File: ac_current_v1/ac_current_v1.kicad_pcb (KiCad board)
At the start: 2 copper layers, 107.7 x 89.4 mm, 35 parts, among them J1 ICSP, J2 UART, J3 AC1_IN, J4 AC1_OUT, J5 AC2_IN, J6 AC2_OUT, J7 GMS1012, J8 AC_SLCT_2, J9 AC_SLCT_1, U1 NRF24L01_Breakout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

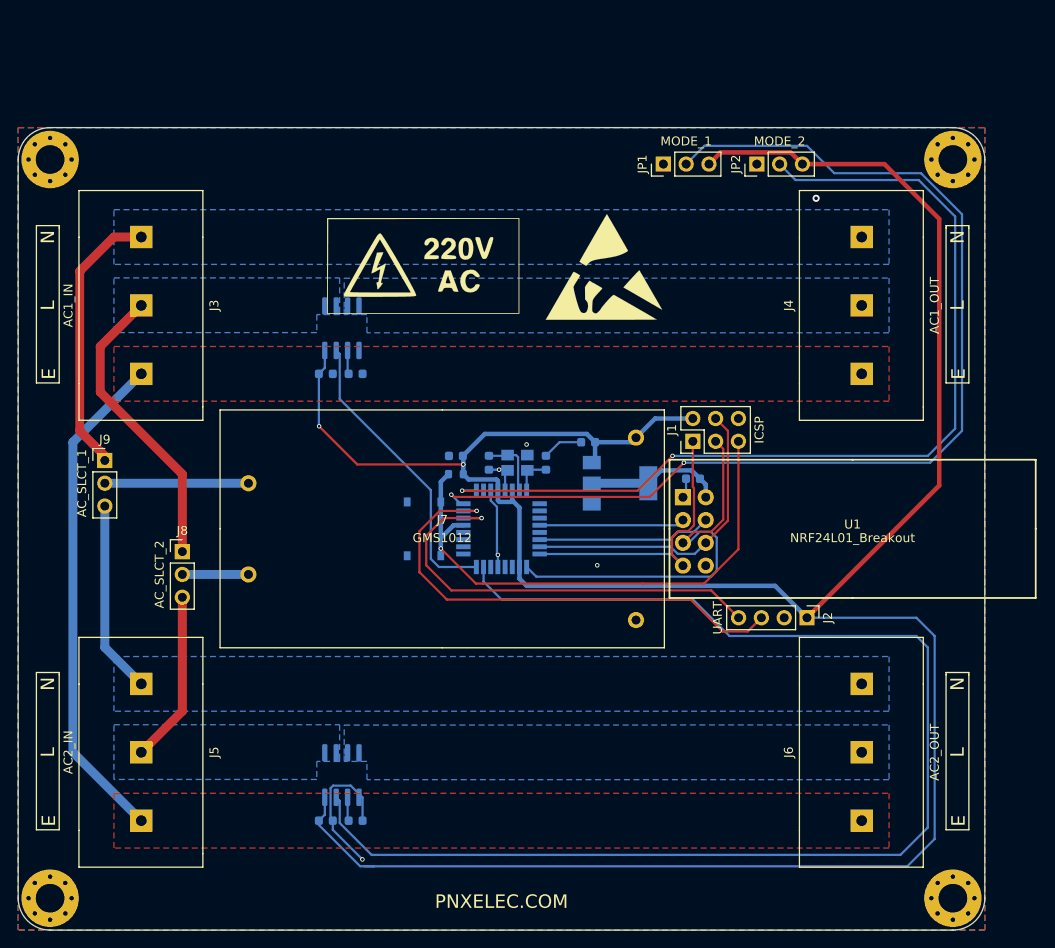
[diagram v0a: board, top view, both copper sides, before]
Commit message: PCB Update(Added Sensor)
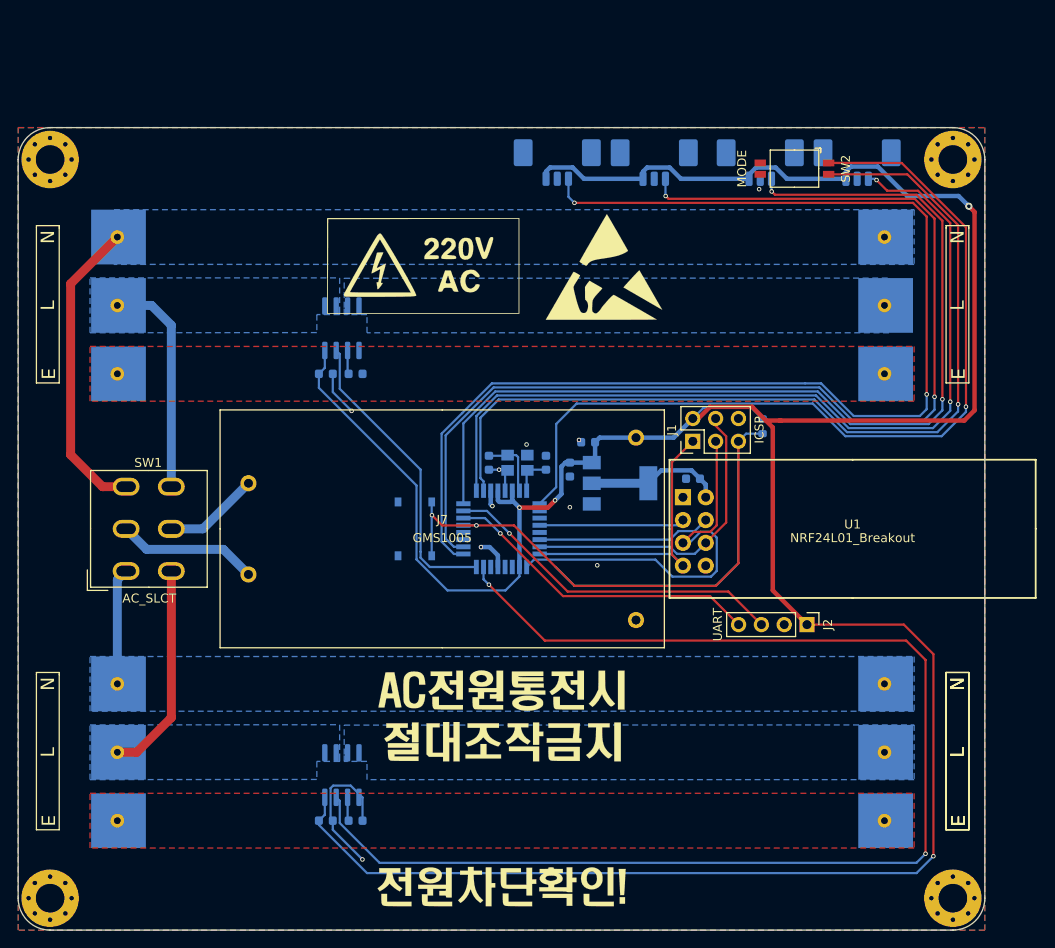
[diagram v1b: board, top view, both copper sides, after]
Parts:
- removed J8: AC_SLCT_2, Connector_PinHeader_2.54mm:PinHeader_1x03_P2.54mm_Vertical
- removed J9: AC_SLCT_1, Connector_PinHeader_2.54mm:PinHeader_1x03_P2.54mm_Vertical
- removed JP1: MODE_1, Connector_PinHeader_2.54mm:PinHeader_1x03_P2.54mm_Vertical
- removed JP2: MODE_2, Connector_PinHeader_2.54mm:PinHeader_1x03_P2.54mm_Vertical
- added G***: LOGO, KIcad:caution2, F.Cu at (150.2, 140.1)
- added G***: LOGO, KIcad:caution, F.Cu at (150.2, 121.0)
- added J10: Flow_1, Connector_Molex:Molex_PicoBlade_53261-0371_1x03-1MP_P1.25mm_Horizontal, B.Cu at (189.9, 58.8)
- added J11: Flow_2, Connector_Molex:Molex_PicoBlade_53261-0371_1x03-1MP_P1.25mm_Horizontal, B.Cu at (179.1, 58.8)
- added J12: NC_Liquid_1, Connector_Molex:Molex_PicoBlade_53261-0371_1x03-1MP_P1.25mm_Horizontal, B.Cu at (167.3, 58.8)
- added J13: NC_Liquid_2, Connector_Molex:Molex_PicoBlade_53261-0371_1x03-1MP_P1.25mm_Horizontal, B.Cu at (156.5, 58.8)
- added SW1: AC_SLCT, KIcad:MTS-202, F.Cu at (111.0, 100.2)
- added SW2: MODE, KIcad:DSHP02TSGER, F.Cu at (182.9, 60.1)
- J3, J4, J5, J6: footprint KIcad:BR-762C_3 -> KIcad:SMD_762; moved to B.Cu
- J7: value GMS1012 -> GMS1005
- moved R1 34.6 mm to (179.3, 88.8), turned to 90 degrees
- moved C3 12.8 mm to (157.9, 93.6), turned to 90 degrees
- moved J4 5.20 mm to (193.0, 75.3)
- moved J6 5.20 mm to (193.0, 125.1)
- moved S1 1.02 mm to (140.6, 100.2)
- moved J2 0.76 mm to (184.3, 110.9)
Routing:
- net /A2: track 0.00 -> 137.5 mm, vias 0 -> 2
- net /A3: track 0.00 -> 126.7 mm, vias 0 -> 2
- net /D4: track 0.00 -> 102.3 mm, vias 0 -> 1
- net /D5: track 0.00 -> 97.7 mm, vias 0 -> 1
- net Earth: track 56.1 -> 0.00 mm
- net /RST: track 60.9 -> 98.5 mm, vias 1 -> 2
- net +5V: track 304.9 -> 337.3 mm, vias 2 -> 4
- net /TX: track 54.8 -> 38.5 mm
- net /RX: track 49.5 -> 35.6 mm
- net /D2: track 120.7 -> 108.8 mm
- net /D3: track 105.0 -> 96.5 mm
- net Net-(J5-Pad3): track 21.5 -> 13.0 mm
- net Net-(J7-Pad2): track 7.37 -> 15.7 mm
- net Net-(J3-Pad2): track 33.1 -> 24.9 mm
- net Net-(J7-Pad1): track 16.0 -> 10.7 mm
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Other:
- board text removed: "PNXELEC.COM"

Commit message: PCB Update
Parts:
- removed the G*** at (190.4, 100.2)
- removed J7: GMS1005, KIcad:GMS1012
- removed SW1: AC_SLCT, KIcad:MTS-202
- removed SW2: MODE, KIcad:DSHP02TSGER
- added C10: 10uf, Capacitor_Tantalum_SMD:CP_EIA-3216-18_Kemet-A, B.Cu at (178.8, 120.5)
- added C15: 100nf, Capacitor_SMD:C_0603_1608Metric, B.Cu at (167.1, 122.3)
- added D1: Flow2, LED_THT:LED_D3.0mm, F.Cu at (140.7, 119.6)
- added D2: Flow1, LED_THT:LED_D3.0mm, F.Cu at (133.1, 119.6)
- added D3: Drain2, LED_THT:LED_D3.0mm, F.Cu at (140.7, 112.2)
- added D4: Drain1, LED_THT:LED_D3.0mm, F.Cu at (133.1, 112.2)
- added D5: Current2, LED_THT:LED_D3.0mm, F.Cu at (140.7, 104.8)
- added D6: Current1, LED_THT:LED_D3.0mm, F.Cu at (133.1, 104.8)
- added D7: 5V, LED_THT:LED_D3.0mm, F.Cu at (133.6, 127.9)
- added G***: LOGO, KIcad:qrcode, F.Cu at (118.4, 114.7)
- added J14: MODE_2, Connector_PinHeader_2.54mm:PinHeader_1x03_P2.54mm_Vertical, F.Cu at (151.1, 109.6)
- added J8: DEBUG_MODE, Connector_PinHeader_2.54mm:PinHeader_1x03_P2.54mm_Vertical, F.Cu at (145.7, 103.0)
- added J9: MODE_1, Connector_PinHeader_2.54mm:PinHeader_1x03_P2.54mm_Vertical, F.Cu at (145.3, 109.6)
- added PS1: GMS0205, KIcad:GMS0205, F.Cu at (118.5, 114.8)
- added R2: 330, Resistor_SMD:R_0603_1608Metric, B.Cu at (136.2, 118.8)
- added R3: 330, Resistor_SMD:R_0603_1608Metric, B.Cu at (128.6, 118.8)
- added R4: 330, Resistor_SMD:R_0603_1608Metric, B.Cu at (136.2, 111.4)
- added R5: 330, Resistor_SMD:R_0603_1608Metric, B.Cu at (128.6, 111.4)
- added R6: 330, Resistor_SMD:R_0603_1608Metric, B.Cu at (136.2, 104.0)
- added R7: 330, Resistor_SMD:R_0603_1608Metric, B.Cu at (128.6, 104.0)
- added R8: 330, Resistor_SMD:R_0603_1608Metric, B.Cu at (128.6, 127.4)
- added REF**: SMD_762_MountHole, KIcad:SMD_762_MountHole, F.Cu at (105.7, 86.9)
- added REF**: SMD_762_MountHole, KIcad:SMD_762_MountHole, F.Cu at (105.7, 62.0)
- added REF**: SMD_762_MountHole, KIcad:SMD_762_MountHole, F.Cu at (189.0, 86.9)
- added REF**: SMD_762_MountHole, KIcad:SMD_762_MountHole, F.Cu at (189.0, 62.0)
- added U6: 74HC595, Package_SO:SO-16_3.9x9.9mm_P1.27mm, B.Cu at (161.0, 120.1)
- C1, C2: value 100nf -> 10uf; footprint Capacitor_SMD:C_0603_1608Metric -> Capacitor_Tantalum_SMD:CP_EIA-3216-18_Kemet-A
- H1, H2, H3, H4: footprint MountingHole:MountingHole_3.2mm_M3_Pad_Via -> MountingHole:MountingHole_3.2mm_M3
- J12: value NC_Liquid_1 -> Drain_1
- J13: value NC_Liquid_2 -> Drain_2
- J3: value AC1_IN -> AC2_IN
- J4: value AC1_OUT -> AC2_OUT
- J5: value AC2_IN -> AC1_IN
- J6: value AC2_OUT -> AC1_OUT
- R1: value 1k -> 10k
- U1: value NRF24L01_Breakout -> GT-24; footprint KIcad:NRF24L01_PA_LNA -> KIcad:nrf24l01 smd
- U2: value AMS1117-3.3 -> NCP603SN330; footprint Package_TO_SOT_SMD:SOT-223-3_TabPin2 -> Package_SO:TSOP-5_1.65x3.05mm_P0.95mm
- moved G*** 92.5 mm to (147.5, 47.6)
- moved J10 83.3 mm to (144.8, 128.8), turned to 180 degrees
- moved J13 73.7 mm to (179.4, 128.8), turned to 180 degrees
- moved J11 73.6 mm to (156.3, 128.8), turned to 180 degrees
- moved J12 70.0 mm to (167.9, 128.8), turned to 180 degrees
- moved C8 47.5 mm to (158.9, 94.6)
- moved C9 47.5 mm to (162.2, 94.6)
- moved U5 47.5 mm to (160.7, 89.5)
- moved J2 40.9 mm to (144.3, 119.6), turned to 90 degrees
- moved J6 39.9 mm to (181.3, 86.9)
- moved G*** 39.0 mm to (147.5, 82.1)
- moved J5 38.7 mm to (113.9, 86.9)
- moved C1 31.8 mm to (170.4, 120.6), turned to 90 degrees
- moved C6 31.2 mm to (158.9, 69.7)
- moved C7 31.2 mm to (162.2, 69.7)
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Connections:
- net Net-(J5-Pad2) renamed NEUT
- net Net-(J5-Pad3) renamed LINE
- net Net-(U3-Pad19) renamed /A6
- net Net-(U3-Pad22) renamed /A7
- H1 pad 1: GND -> Net-(H1-Pad1)
- H2 pad 1: GND -> Net-(H2-Pad1)
- H3 pad 1: GND -> Net-(H3-Pad1)
- H4 pad 1: GND -> Net-(H4-Pad1)
- J12 pad 3: /A3 -> /A0
- J13 pad 3: /A2 -> /A1
- J3 pad 1: Earth -> GND1
- J4 pad 1: Earth -> GND1
- J5 pad 1: Earth -> GND2
- J6 pad 1: Earth -> GND2
- U1 pad 1: GND -> +3V3
- U1 pad 2: +3V3 -> /D8
- U1 pad 3: /D8 -> /D10
- U1 pad 4: /D10 -> /D13
- U1 pad 5: /D13 -> /D11
- U1 pad 6: /D11 -> /D12
- U1 pad 7: /D12 -> Net-(U1-Pad7)
- U1 pad 8: Net-(U1-Pad8) -> GND
- U2 pad 1: GND -> +5V
- U2 pad 2: +3V3 -> GND
- U2 pad 3: +5V -> /D4
- U4 pad 7: /A1 -> /A4
- U5 pad 7: /A0 -> /A5
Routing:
- net /A2: track 137.5 -> 13.4 mm, vias 2 -> 1
- net /A0: track 146.5 -> 22.9 mm
- net /A3: track 126.7 -> 6.96 mm, vias 2 -> 1
- net /A4: track 0.00 -> 117.2 mm, vias 0 -> 2
- net /D2: track 108.8 -> 22.0 mm
- net /D4: track 102.3 -> 27.5 mm, vias 1 -> 2
- net /RST: track 98.5 -> 24.6 mm
- net +5V: track 337.3 -> 263.8 mm, vias 4 -> 3
- net /D5: track 97.7 -> 24.4 mm, vias 1 -> 2
- net /D3: track 96.5 -> 33.6 mm
- net Net-(R7-Pad1): track 0.00 -> 62.3 mm
- net Net-(R5-Pad1): track 0.00 -> 52.6 mm
- net Net-(R6-Pad1): track 0.00 -> 49.4 mm
- net GND: track 31.1 -> 78.9 mm, vias 10 -> 9
- net /A5: track 0.00 -> 44.1 mm, vias 0 -> 2
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- added copper zone on B.Cu, net +3V3
- added copper zone on B.Cu, net +5V
- added copper zone on F.Cu, net GND1
- added copper zone on F.Cu, net GND2
- removed copper zone on F.Cu, net Earth
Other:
- board size 107.7 x 89.4 mm -> 89.6 x 89.4 mm
- board text added: "+"
- board text added: "5V"
- board text added: "CH1"
- board text added: "CH2"
- board text added: "Debug"
- board text added: "Drain_1"
- board text added: "Drain_2"
- board text added: "Dry"
- board text added: "Flow_1"
- board text added: "Flow_2"
- board text added: "G"
- board text added: "Normal"
- board text added: "RX"
- board text added: "TX"
- board text added: "Wsh"
